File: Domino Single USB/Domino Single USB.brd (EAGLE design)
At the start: 25.4 x 33 mm, 22 parts, among them J1 MH10-1, J2 USB_AF-006, J3 MH10-1

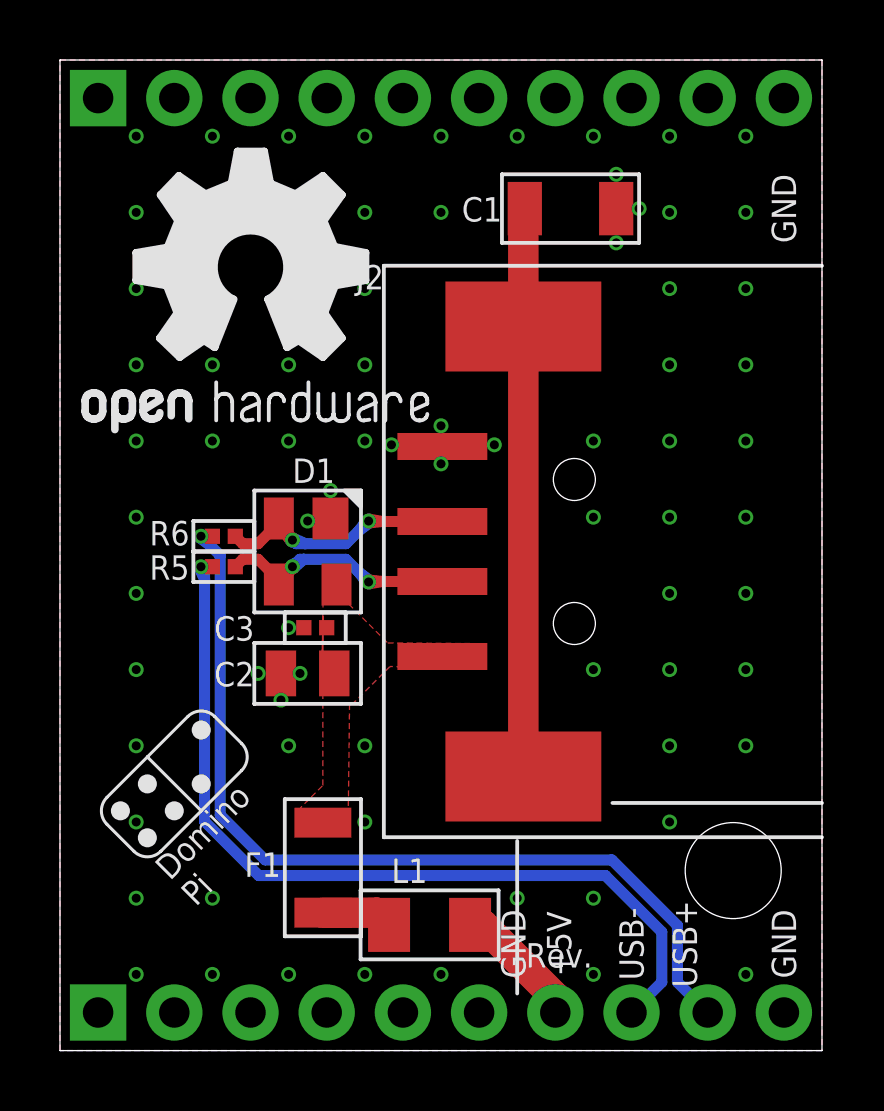
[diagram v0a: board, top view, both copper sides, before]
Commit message: Re-routed Single USB tile to remove vias on USB traces
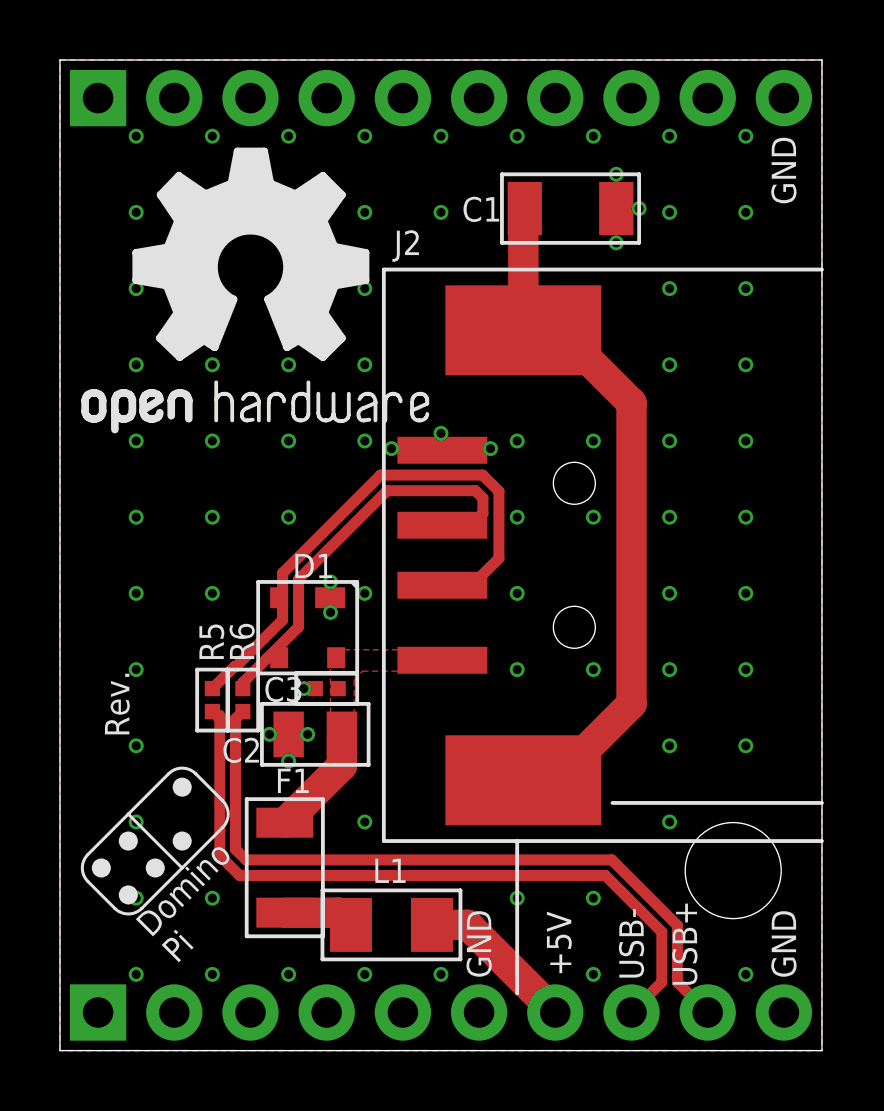
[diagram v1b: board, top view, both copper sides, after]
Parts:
- moved R6 5.50 mm to (6.10, 11.7), turned to 270 degrees
- moved R5 4.46 mm to (5.08, 11.7), turned to 270 degrees
- moved D1 2.54 mm to (8.26, 14.1)
- moved C3 2.07 mm to (8.89, 12.1)
- moved C2 2.05 mm to (8.51, 10.5)
- moved U$10 2.01 mm to (3.17, 6.99)
- moved L1 1.27 mm to (11.0, 4.19)
- moved F1 1.27 mm to (7.49, 6.10)
- moved J2 0.13 mm to (17.1, 16.5)
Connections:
- net D_N: now also D1.2; no longer D1.3
- net D_P: now also D1.3; no longer D1.2
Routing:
- net USB_P: track 31.0 -> 23.8 mm, vias 1 -> 0
- net D_N: track 12.3 -> 18.3 mm, vias 2 -> 0
- net USB_N: track 29.8 -> 23.9 mm, vias 1 -> 0
- net PE: track 19.0 -> 23.5 mm
- net VBUS: track 0.00 -> 3.73 mm
- net D_P: track 12.2 -> 14.3 mm, vias 2 -> 0
- net +5V: track 4.35 -> 5.32 mm

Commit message: Domino Single USB Rev. C: changed Logos
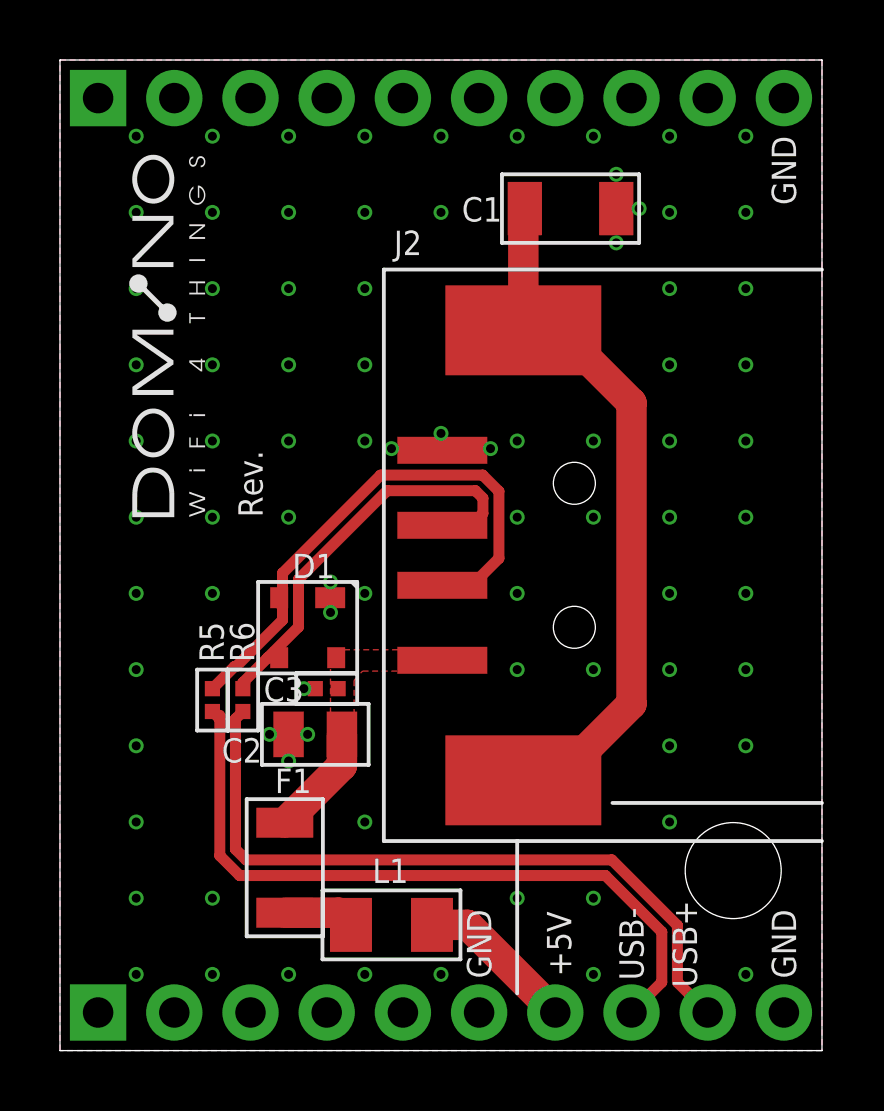
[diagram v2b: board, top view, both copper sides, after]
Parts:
- removed U$13: (no value), Domino:OPEN_HARDWARE_LOGO
- added U$7: DOMINO_LOGO, Domino:DOMINO_LOGO
- moved U$11 11.4 mm to (14.0, 6.35)
- moved U$10 10.8 mm to (3.81, 17.8), turned to 90 degrees
- moved U$4 9.52 mm to (22.9, 16.5)
- moved U$8 1.27 mm to (5.71, 3.81)
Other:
- board text removed: "Domino Core"
- board text removed: "Domino Pi"
- board text removed: "Domino Qi"
